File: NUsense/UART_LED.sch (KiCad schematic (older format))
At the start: 5 parts, among them U2? SM712

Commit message: Change hierarchy layout
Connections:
- net labels added: +3.3V
- net labels removed: VDD3o3V
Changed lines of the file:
@@
 LIBS:valves
 LIBS:ADM6713RAKS
+LIBS:Header_Connectors
 LIBS:MPU6000
 LIBS:NUbots
 LIBS:STM32F746ZGT6
-LIBS:Header_Connectors
 LIBS:NUsense-cache
 EELAYER 25 0
@@
 Comment4 ""
 $EndDescr
-Text GLabel 2100 1800 0    60   Input ~ 0
-VDD3o3V
 $Comp
 L R R?
@@
 	1    0    0    -1
 $EndComp
-Text GLabel 4800 1250 1    60   Input ~ 0
-VDD3o3V
 Wire Wire Line
 	3800 1900 3900 1900
@@
 Wire Wire Line
 	4800 2050 4800 2250
-Text GLabel 2100 1450 0    60   Input ~ 0
+$Comp
+L +3.3V #PWR?
+U 1 1 5A6FD7BD
+P 4800 1250
+F 0 "#PWR?" H 4800 1100 50  0001 C CNN
+F 1 "+3.3V" H 4800 1390 50  0000 C CNN
+F 2 "" H 4800 1250 50  0001 C CNN
+F 3 "" H 4800 1250 50  0001 C CNN
+	1    4800 1250
+	1    0    0    -1
+$EndComp
+$Comp
+L +3.3V #PWR?
+U 1 1 5A6FD880
+P 2100 1800
+F 0 "#PWR?" H 2100 1650 50  0001 C CNN
+F 1 "+3.3V" H 2100 1940 50  0000 C CNN
+F 2 "" H 2100 1800 50  0001 C CNN
+F 3 "" H 2100 1800 50  0001 C CNN
+	1    2100 1800
+	0    -1   -1   0
+$EndComp
+Text HLabel 2100 1450 0    60   Input ~ 0
 USER_UART_RX
-Text GLabel 2100 1550 0    60   Input ~ 0
+Text HLabel 2100 1550 0    60   Output ~ 0
 USER_UART_TX
 $EndSCHEMATC

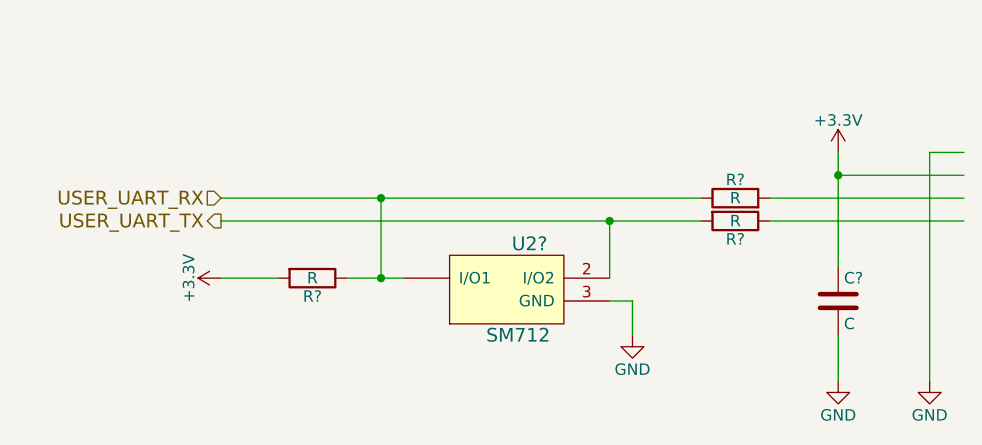
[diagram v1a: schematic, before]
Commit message: Update component values
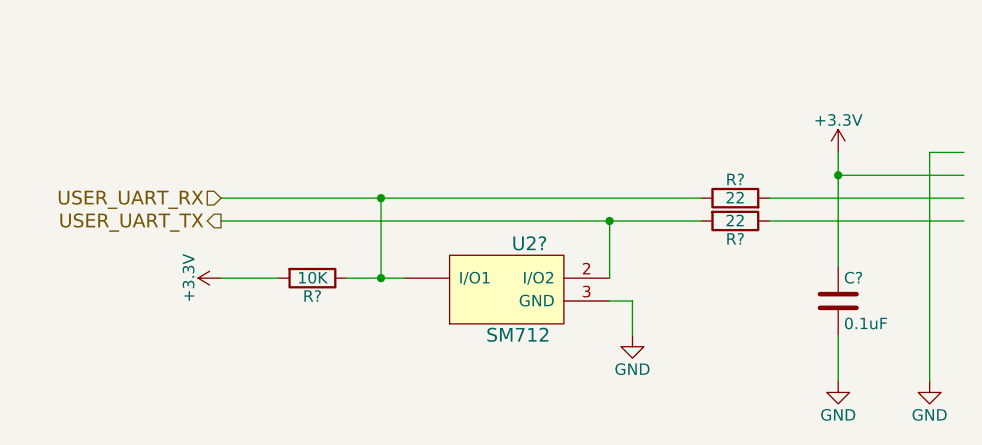
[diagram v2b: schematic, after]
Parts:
- C?: value C -> 0.1uF
- R?: value R -> 10K
- R? (x2): value R -> 22
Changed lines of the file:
@@
 P 2500 1800
 F 0 "R?" V 2580 1800 50  0000 C CNN
-F 1 "R" V 2500 1800 50  0000 C CNN
+F 1 "10K" V 2500 1800 50  0000 C CNN
 F 2 "" V 2430 1800 50  0001 C CNN
 F 3 "" H 2500 1800 50  0001 C CNN
@@
 P 4350 1550
 F 0 "R?" V 4430 1550 50  0000 C CNN
-F 1 "R" V 4350 1550 50  0000 C CNN
+F 1 "22" V 4350 1550 50  0000 C CNN
 F 2 "" V 4280 1550 50  0001 C CNN
 F 3 "" H 4350 1550 50  0001 C CNN
@@
 P 4350 1450
 F 0 "R?" V 4430 1450 50  0000 C CNN
-F 1 "R" V 4350 1450 50  0000 C CNN
+F 1 "22" V 4350 1450 50  0000 C CNN
 F 2 "" V 4280 1450 50  0001 C CNN
 F 3 "" H 4350 1450 50  0001 C CNN
@@
 P 4800 1900
 F 0 "C?" H 4825 2000 50  0000 L CNN
-F 1 "C" H 4825 1800 50  0000 L CNN
+F 1 "0.1uF" H 4825 1800 50  0000 L CNN
 F 2 "" H 4838 1750 50  0001 C CNN
 F 3 "" H 4800 1900 50  0001 C CNN
